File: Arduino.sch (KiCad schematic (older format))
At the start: 19 parts

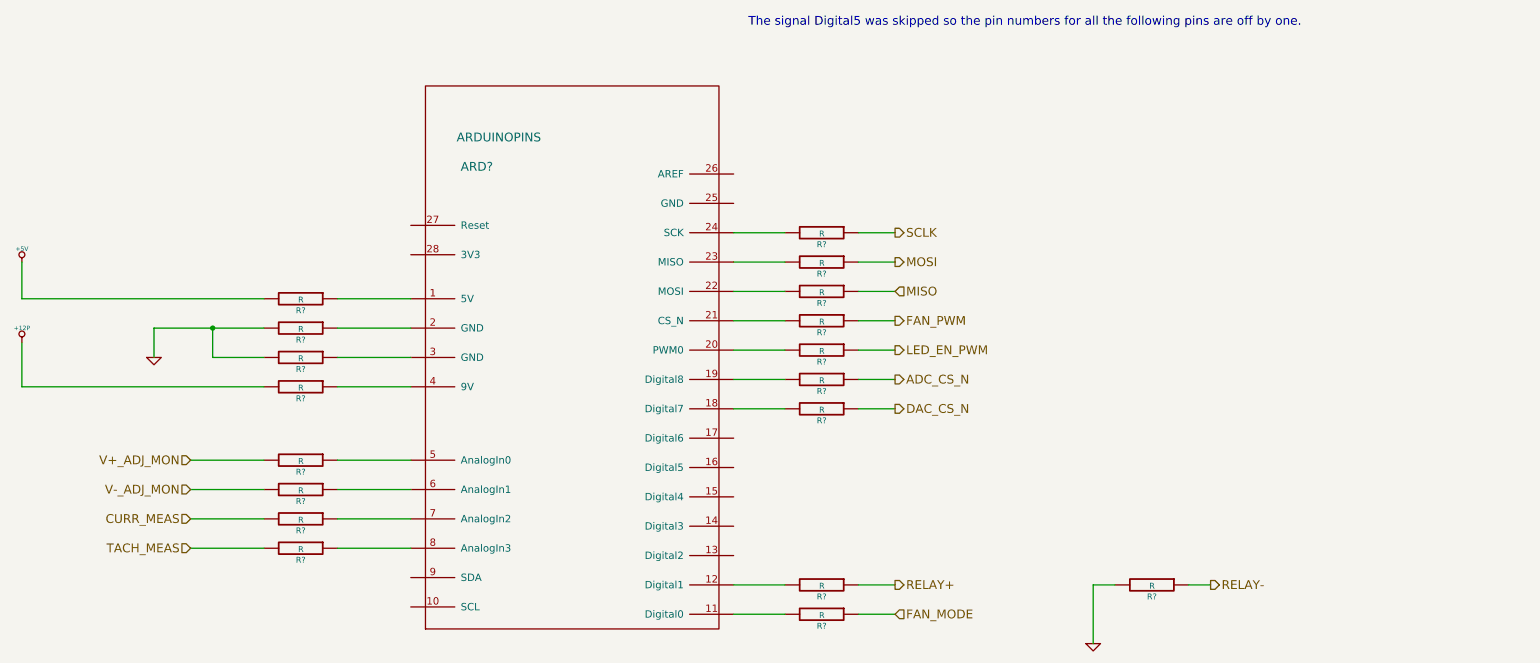
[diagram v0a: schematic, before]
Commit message: Created Footprints and Placed Relay Module
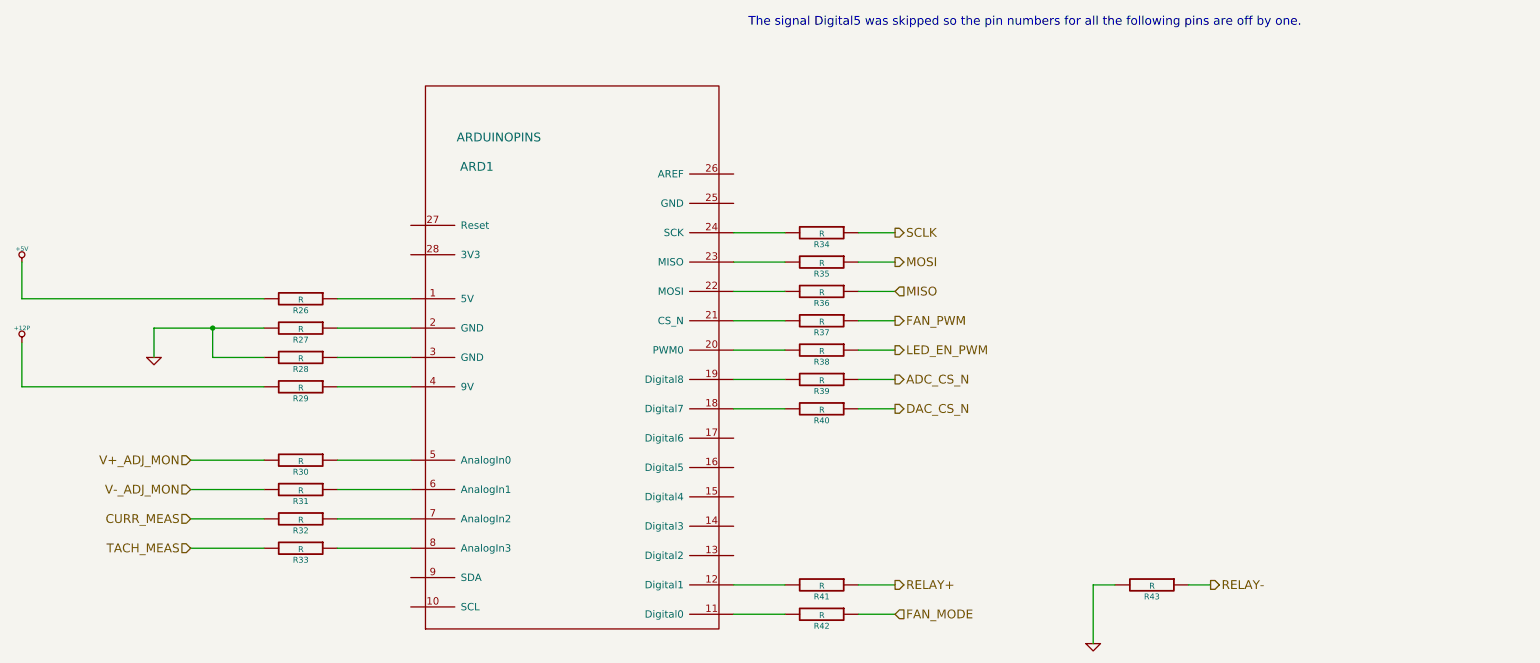
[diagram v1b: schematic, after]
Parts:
- gave numbers to parts that had none: 19
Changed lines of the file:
@@
-EESchema Schematic File Version 2  date 10/10/2013 12:18:22 AM
+EESchema Schematic File Version 2  date 10/10/2013 1:06:29 AM
 LIBS:power
 LIBS:device
@@
 CURR_MEAS
 $Comp
-L R R?
+L R R37
 U 1 1 52400F4A
 P 6650 3900
-F 0 "R?" V 6730 3900 40  0000 C CNN
+F 0 "R37" V 6730 3900 40  0000 C CNN
 F 1 "R" V 6657 3901 40  0000 C CNN
 F 2 "~" V 6580 3900 30  0000 C CNN
@@
 	6400 3900 6050 3900
 $Comp
-L R R?
+L R R41
 U 1 1 52400F79
 P 6650 5700
-F 0 "R?" V 6730 5700 40  0000 C CNN
+F 0 "R41" V 6730 5700 40  0000 C CNN
 F 1 "R" V 6657 5701 40  0000 C CNN
 F 2 "~" V 6580 5700 30  0000 C CNN
@@
 	8500 5700 8500 6100
 $Comp
-L GND #PWR?
+L GND #PWR55
 U 1 1 524020EC
 P 8500 6100
-F 0 "#PWR?" H 8500 6100 30  0001 C CNN
+F 0 "#PWR55" H 8500 6100 30  0001 C CNN
 F 1 "GND" H 8500 6030 30  0001 C CNN
 F 2 "~" H 8500 6100 60  0000 C CNN
@@
 $EndComp
 $Comp
-L R R?
+L R R32
 U 1 1 52402349
 P 3100 5250
-F 0 "R?" V 3180 5250 40  0000 C CNN
+F 0 "R32" V 3180 5250 40  0000 C CNN
 F 1 "R" V 3107 5251 40  0000 C CNN
 F 2 "~" V 3030 5250 30  0000 C CNN
@@
 $EndComp
 $Comp
-L R R?
+L R R33
 U 1 1 5240234F
 P 3100 5450
-F 0 "R?" V 3180 5450 40  0000 C CNN
+F 0 "R33" V 3180 5450 40  0000 C CNN
 F 1 "R" V 3107 5451 40  0000 C CNN
 F 2 "~" V 3030 5450 30  0000 C CNN
@@
 V-_ADJ_MON
 $Comp
-L R R?
+L R R31
 U 1 1 52402CCD
 P 3100 5050
-F 0 "R?" V 3180 5050 40  0000 C CNN
+F 0 "R31" V 3180 5050 40  0000 C CNN
 F 1 "R" V 3107 5051 40  0000 C CNN
 F 2 "~" V 3030 5050 30  0000 C CNN
@@
 	2850 5050 2350 5050
 $Comp
-L R R?
+L R R30
 U 1 1 52402D06
 P 3100 4850
-F 0 "R?" V 3180 4850 40  0000 C CNN
+F 0 "R30" V 3180 4850 40  0000 C CNN
 F 1 "R" V 3107 4851 40  0000 C CNN
 F 2 "~" V 3030 4850 30  0000 C CNN
@@
 	3350 4850 3850 4850
 $Comp
-L R R?
+L R R34
 U 1 1 52402D2F
 P 6650 3300
-F 0 "R?" V 6730 3300 40  0000 C CNN
+F 0 "R34" V 6730 3300 40  0000 C CNN
 F 1 "R" V 6657 3301 40  0000 C CNN
 F 2 "~" V 6580 3300 30  0000 C CNN
@@
 $EndComp
 $Comp
-L R R?
+L R R35
 U 1 1 52402D35
 P 6650 3500
-F 0 "R?" V 6730 3500 40  0000 C CNN
+F 0 "R35" V 6730 3500 40  0000 C CNN
 F 1 "R" V 6657 3501 40  0000 C CNN
 F 2 "~" V 6580 3500 30  0000 C CNN
@@
 $EndComp
 $Comp
-L R R?
+L R R36
 U 1 1 52402D3B
 P 6650 3700
-F 0 "R?" V 6730 3700 40  0000 C CNN
+F 0 "R36" V 6730 3700 40  0000 C CNN
 F 1 "R" V 6657 3701 40  0000 C CNN
 F 2 "~" V 6580 3700 30  0000 C CNN
@@
 $EndComp
 $Comp
-L R R?
+L R R40
 U 1 1 52402D41
 P 6650 4500
-F 0 "R?" V 6730 4500 40  0000 C CNN
+F 0 "R40" V 6730 4500 40  0000 C CNN
 F 1 "R" V 6657 4501 40  0000 C CNN
 F 2 "~" V 6580 4500 30  0000 C CNN
@@
 	6400 4500 6050 4500
 $Comp
-L R R?
+L R R43
 U 1 1 52402DDB
 P 8900 5700
-F 0 "R?" V 8980 5700 40  0000 C CNN
+F 0 "R43" V 8980 5700 40  0000 C CNN
 F 1 "R" V 8907 5701 40  0000 C CNN
 F 2 "~" V 8830 5700 30  0000 C CNN
@@
 LED_EN_PWM
 $Comp
-L R R?
+L R R38
 U 1 1 52402E11
 P 6650 4100
-F 0 "R?" V 6730 4100 40  0000 C CNN
+F 0 "R38" V 6730 4100 40  0000 C CNN
 F 1 "R" V 6657 4101 40  0000 C CNN
 F 2 "~" V 6580 4100 30  0000 C CNN
@@
 	6400 4100 6050 4100
 $Comp
-L R R?
+L R R39
 U 1 1 5240769E
 P 6650 4300
-F 0 "R?" V 6730 4300 40  0000 C CNN
+F 0 "R39" V 6730 4300 40  0000 C CNN
 F 1 "R" V 6657 4301 40  0000 C CNN
 F 2 "~" V 6580 4300 30  0000 C CNN
@@
 FAN_MODE
 $Comp
-L R R?
+L R R42
 U 1 1 5243CF0D
 P 6650 5900
-F 0 "R?" V 6730 5900 40  0000 C CNN
+F 0 "R42" V 6730 5900 40  0000 C CNN
 F 1 "R" V 6657 5901 40  0000 C CNN
 F 2 "~" V 6580 5900 30  0000 C CNN
@@
 	6400 5900 6050 5900
 $Comp
-L R R?
+L R R29
 U 1 1 5243CF86
 P 3100 4350
-F 0 "R?" V 3180 4350 40  0000 C CNN
+F 0 "R29" V 3180 4350 40  0000 C CNN
 F 1 "R" V 3107 4351 40  0000 C CNN
 F 2 "~" V 3030 4350 30  0000 C CNN
@@
 	3350 4350 3850 4350
 $Comp
-L +12P #PWR?
+L +12P #PWR53
 U 1 1 5243CFCD
 P 1200 4050
-F 0 "#PWR?" H 1200 4020 30  0001 C CNN
+F 0 "#PWR53" H 1200 4020 30  0001 C CNN
 F 1 "+12P" H 1200 4150 30  0000 C CNN
 F 2 "~" H 1200 4050 60  0000 C CNN
@@
 	1200 4350 2850 4350
 $Comp
-L R R?
+L R R26
 U 1 1 5245171E
 P 3100 3750
-F 0 "R?" V 3180 3750 40  0000 C CNN
+F 0 "R26" V 3180 3750 40  0000 C CNN
 F 1 "R" V 3107 3751 40  0000 C CNN
 F 2 "~" V 3030 3750 30  0000 C CNN
@@
 	3350 3750 3850 3750
 $Comp
-L +5V #PWR?
+L +5V #PWR52
 U 1 1 5245176C
 P 1200 3500
-F 0 "#PWR?" H 1200 3590 20  0001 C CNN
+F 0 "#PWR52" H 1200 3590 20  0001 C CNN
 F 1 "+5V" H 1200 3590 30  0000 C CNN
 F 2 "~" H 1200 3500 60  0000 C CNN
@@
 	3850 3950 3350 3950
 $Comp
-L R R?
+L R R27
 U 1 1 524517C0
 P 3100 3950
-F 0 "R?" V 3180 3950 40  0000 C CNN
+F 0 "R27" V 3180 3950 40  0000 C CNN
 F 1 "R" V 3107 3951 40  0000 C CNN
 F 2 "~" V 3030 3950 30  0000 C CNN
@@
 $EndComp
 $Comp
-L R R?
+L R R28
 U 1 1 524517C6
 P 3100 4150
-F 0 "R?" V 3180 4150 40  0000 C CNN
+F 0 "R28" V 3180 4150 40  0000 C CNN
 F 1 "R" V 3107 4151 40  0000 C CNN
 F 2 "~" V 3030 4150 30  0000 C CNN
@@
 	2100 3950 2100 4150
 $Comp
-L GND #PWR?
+L GND #PWR54
 U 1 1 5245181B
 P 2100 4150
-F 0 "#PWR?" H 2100 4150 30  0001 C CNN
+F 0 "#PWR54" H 2100 4150 30  0001 C CNN
 F 1 "GND" H 2100 4080 30  0001 C CNN
 F 2 "~" H 2100 4150 60  0000 C CNN
@@
 The signal Digital5 was skipped so the pin numbers for all the following pins are off by one.
 $Comp
-L ARDUINOPINS ARD?
+L ARDUINOPINS ARD1
 U 1 1 5251D4C8
 P 4950 4450
-F 0 "ARD?" H 4300 6050 60  0000 C CNN
+F 0 "ARD1" H 4300 6050 60  0000 C CNN
 F 1 "ARDUINOPINS" H 4450 6250 60  0000 C CNN
 F 2 "~" H 5500 3500 60  0000 C CNN

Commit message: Associating Thermocouple Module Components
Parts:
- added R46, R47: R, ~, symbol R
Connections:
- net at ARD1.15 (Digital4): now also R47.2
- net at ARD1.16 (Digital5): now also R46.2
- new net ~DR: R47.1
- new net ~RESET: R46.1
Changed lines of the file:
@@
-EESchema Schematic File Version 2  date 10/10/2013 1:06:29 AM
+EESchema Schematic File Version 2  date 10/11/2013 1:04:35 AM
 LIBS:power
 LIBS:device
@@
 $Descr A4 11693 8268
 encoding utf-8
-Sheet 9 9
+Sheet 7 9
 Title ""
-Date "10 oct 2013"
+Date "11 oct 2013"
 Rev ""
 Comp ""
@@
 	8500 5700 8500 6100
 $Comp
-L GND #PWR55
+L GND #PWR049
 U 1 1 524020EC
 P 8500 6100
-F 0 "#PWR55" H 8500 6100 30  0001 C CNN
+F 0 "#PWR049" H 8500 6100 30  0001 C CNN
 F 1 "GND" H 8500 6030 30  0001 C CNN
 F 2 "~" H 8500 6100 60  0000 C CNN
@@
 	3350 4350 3850 4350
 $Comp
-L +12P #PWR53
+L +12P #PWR050
 U 1 1 5243CFCD
 P 1200 4050
-F 0 "#PWR53" H 1200 4020 30  0001 C CNN
+F 0 "#PWR050" H 1200 4020 30  0001 C CNN
 F 1 "+12P" H 1200 4150 30  0000 C CNN
 F 2 "~" H 1200 4050 60  0000 C CNN
@@
 	3350 3750 3850 3750
 $Comp
-L +5V #PWR52
+L +5V #PWR051
 U 1 1 5245176C
 P 1200 3500
-F 0 "#PWR52" H 1200 3590 20  0001 C CNN
+F 0 "#PWR051" H 1200 3590 20  0001 C CNN
 F 1 "+5V" H 1200 3590 30  0000 C CNN
 F 2 "~" H 1200 3500 60  0000 C CNN
@@
 	2100 3950 2100 4150
 $Comp
-L GND #PWR54
+L GND #PWR052
 U 1 1 5245181B
 P 2100 4150
-F 0 "#PWR54" H 2100 4150 30  0001 C CNN
+F 0 "#PWR052" H 2100 4150 30  0001 C CNN
 F 1 "GND" H 2100 4080 30  0001 C CNN
 F 2 "~" H 2100 4150 60  0000 C CNN
@@
 	1    0    0    -1
 $EndComp
+Text HLabel 7150 4900 2    60   Output ~ 0
+~RESET
+$Comp
+L R R46
+U 1 1 52581128
+P 6650 4900
+F 0 "R46" V 6730 4900 40  0000 C CNN
+F 1 "R" V 6657 4901 40  0000 C CNN
+F 2 "~" V 6580 4900 30  0000 C CNN
+F 3 "~" H 6650 4900 30  0000 C CNN
+	1    6650 4900
+	0    1    1    0
+$EndComp
+Wire Wire Line
+	7150 4900 6900 4900
+Wire Wire Line
+	6400 4900 6050 4900
+Text HLabel 7150 5100 2    60   Output ~ 0
+~DR
+$Comp
+L R R47
+U 1 1 52581131
+P 6650 5100
+F 0 "R47" V 6730 5100 40  0000 C CNN
+F 1 "R" V 6657 5101 40  0000 C CNN
+F 2 "~" V 6580 5100 30  0000 C CNN
+F 3 "~" H 6650 5100 30  0000 C CNN
+	1    6650 5100
+	0    1    1    0
+$EndComp
+Wire Wire Line
+	7150 5100 6900 5100
+Wire Wire Line
+	6400 5100 6050 5100
 $EndSCHEMATC

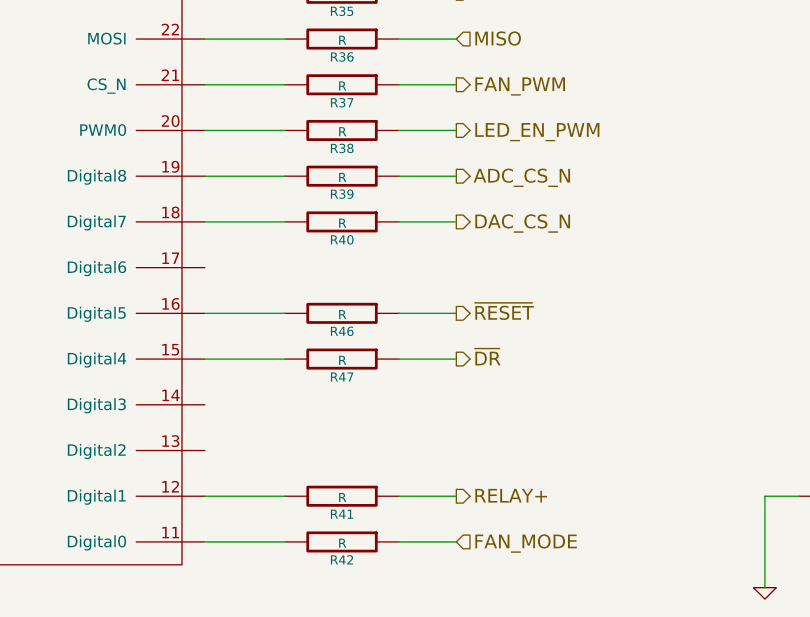
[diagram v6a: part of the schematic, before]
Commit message: Associating Current Module
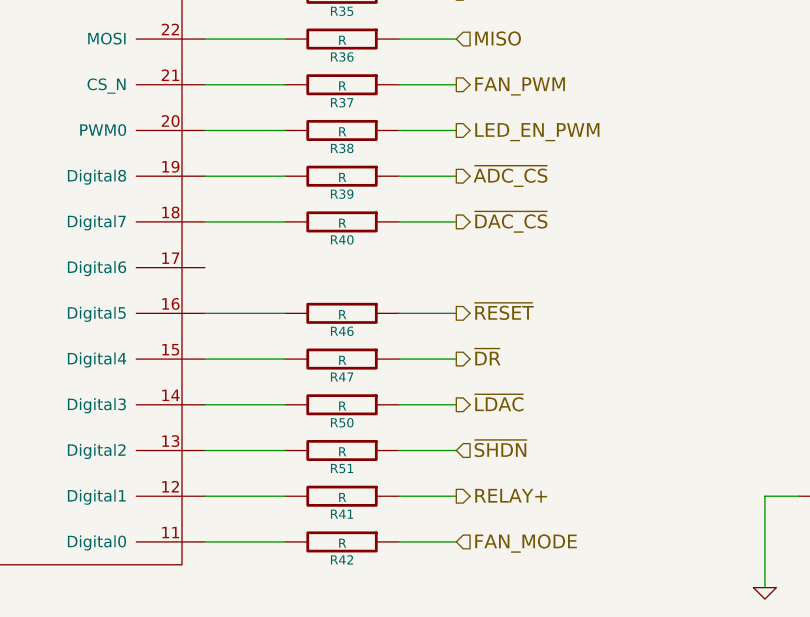
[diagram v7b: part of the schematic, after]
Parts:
- added R50, R51: R, ~, symbol R
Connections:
- net at ARD1.13 (Digital2): now also R51.2
- net at ARD1.14 (Digital3): now also R50.2
- net ADC_CS_N renamed ~ADC_CS
- net DAC_CS_N renamed ~DAC_CS
- new net ~LDAC: R50.1
- new net ~SHDN: R51.1
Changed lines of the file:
@@
-EESchema Schematic File Version 2  date 10/13/2013 2:17:45 PM
+EESchema Schematic File Version 2  date 10/13/2013 8:19:10 PM
 LIBS:power
 LIBS:device
@@
 $Descr A4 11693 8268
 encoding utf-8
-Sheet 7 9
+Sheet 9 9
 Title ""
-Date "13 oct 2013"
+Date "14 oct 2013"
 Rev ""
 Comp ""
@@
 SCLK
 Text HLabel 7150 4500 2    60   Output ~ 0
-DAC_CS_N
+~DAC_CS
 Text HLabel 7150 3900 2    60   Output ~ 0
 FAN_PWM
@@
 	8500 5700 8500 6100
 $Comp
-L GND #PWR55
+L GND #PWR66
 U 1 1 524020EC
 P 8500 6100
-F 0 "#PWR55" H 8500 6100 30  0001 C CNN
+F 0 "#PWR66" H 8500 6100 30  0001 C CNN
 F 1 "GND" H 8500 6030 30  0001 C CNN
 F 2 "~" H 8500 6100 60  0000 C CNN
@@
 	6400 4300 6050 4300
 Text HLabel 7150 4300 2    60   Output ~ 0
-ADC_CS_N
+~ADC_CS
 Wire Wire Line
 	7150 4300 6900 4300
@@
 	3350 4350 3850 4350
 $Comp
-L +12P #PWR53
+L +12P #PWR64
 U 1 1 5243CFCD
 P 1200 4050
-F 0 "#PWR53" H 1200 4020 30  0001 C CNN
+F 0 "#PWR64" H 1200 4020 30  0001 C CNN
 F 1 "+12P" H 1200 4150 30  0000 C CNN
 F 2 "~" H 1200 4050 60  0000 C CNN
@@
 	3350 3750 3850 3750
 $Comp
-L +5V #PWR52
+L +5V #PWR63
 U 1 1 5245176C
 P 1200 3500
-F 0 "#PWR52" H 1200 3590 20  0001 C CNN
+F 0 "#PWR63" H 1200 3590 20  0001 C CNN
 F 1 "+5V" H 1200 3590 30  0000 C CNN
 F 2 "~" H 1200 3500 60  0000 C CNN
@@
 	2100 3950 2100 4150
 $Comp
-L GND #PWR54
+L GND #PWR65
 U 1 1 5245181B
 P 2100 4150
-F 0 "#PWR54" H 2100 4150 30  0001 C CNN
+F 0 "#PWR65" H 2100 4150 30  0001 C CNN
 F 1 "GND" H 2100 4080 30  0001 C CNN
 F 2 "~" H 2100 4150 60  0000 C CNN
@@
 Wire Wire Line
 	6400 5100 6050 5100
+$Comp
+L R R50
+U 1 1 525B3E56
+P 6650 5300
+F 0 "R50" V 6730 5300 40  0000 C CNN
+F 1 "R" V 6657 5301 40  0000 C CNN
+F 2 "~" V 6580 5300 30  0000 C CNN
+F 3 "~" H 6650 5300 30  0000 C CNN
+	1    6650 5300
+	0    1    1    0
+$EndComp
+$Comp
+L R R51
+U 1 1 525B3E5C
+P 6650 5500
+F 0 "R51" V 6730 5500 40  0000 C CNN
+F 1 "R" V 6657 5501 40  0000 C CNN
+F 2 "~" V 6580 5500 30  0000 C CNN
+F 3 "~" H 6650 5500 30  0000 C CNN
+	1    6650 5500
+	0    1    1    0
+$EndComp
+Wire Wire Line
+	6400 5300 6050 5300
+Wire Wire Line
+	6050 5500 6400 5500
+Text HLabel 7150 5300 2    60   Output ~ 0
+~LDAC
+Text HLabel 7150 5500 2    60   Input ~ 0
+~SHDN
+Wire Wire Line
+	7150 5500 6900 5500
+Wire Wire Line
+	6900 5300 7150 5300
 $EndSCHEMATC
